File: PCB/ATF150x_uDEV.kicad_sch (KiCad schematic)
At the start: 14 parts, among them J1 Altera JTAG-A+VPP, J2 VERT, J3 VERT, U1 ATF150x-xAx44

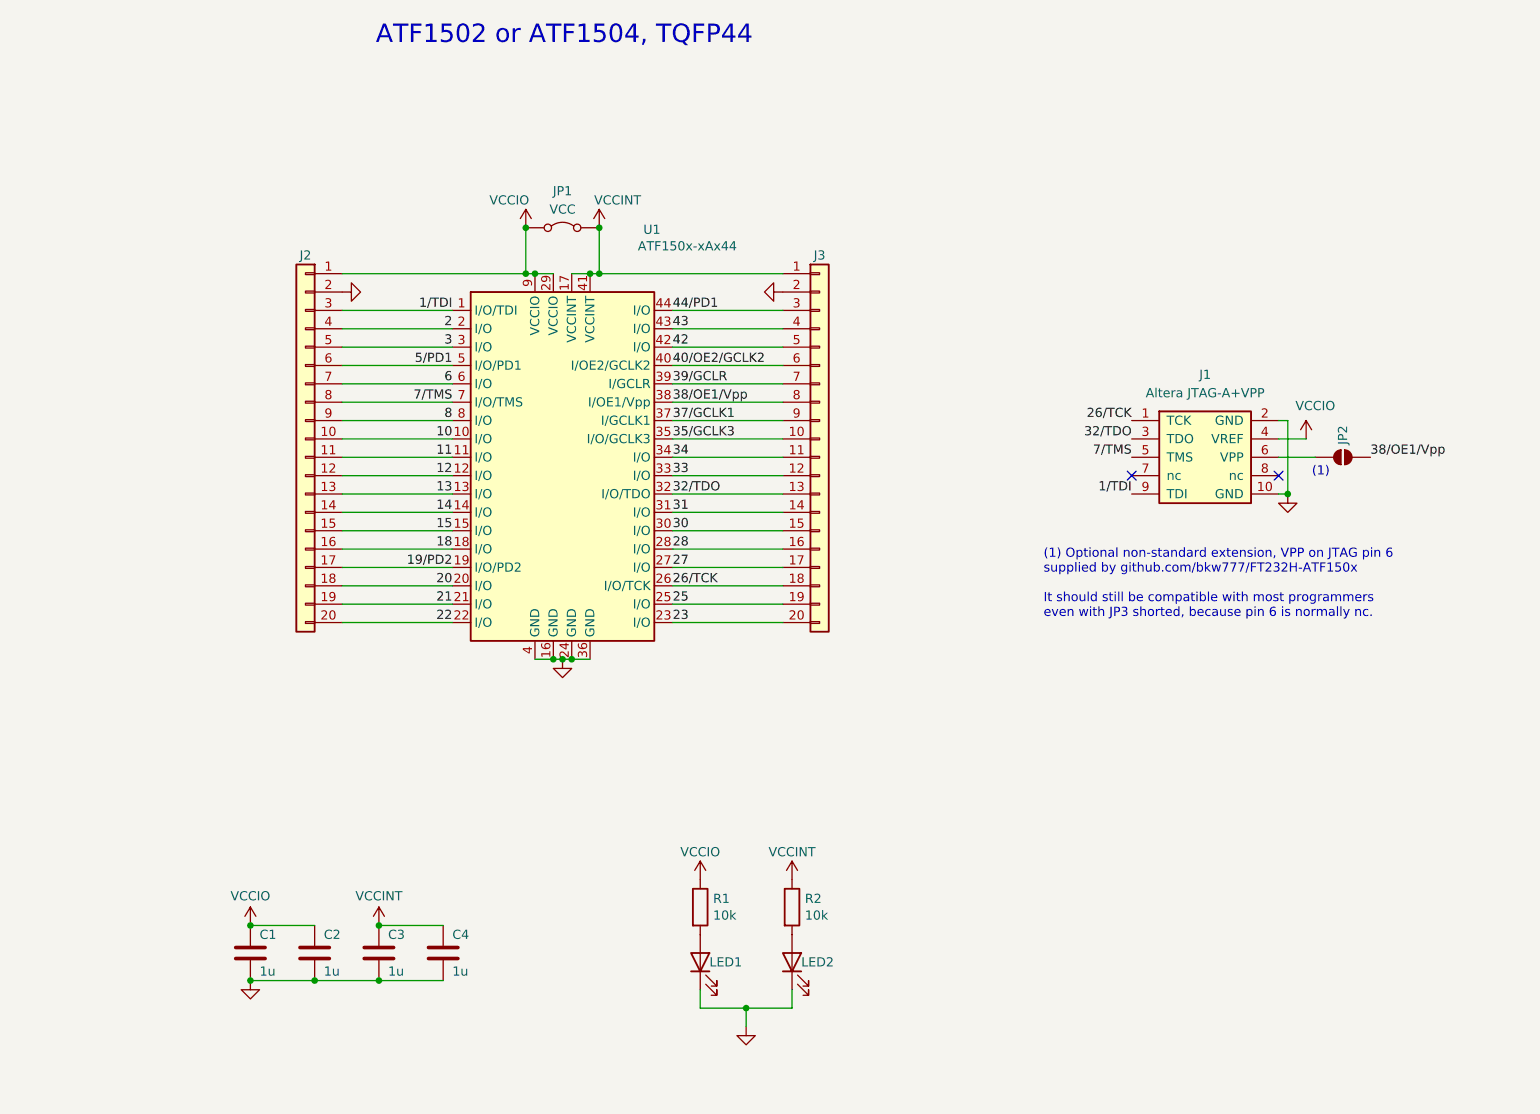
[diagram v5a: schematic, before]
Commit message: update link in comment in sch
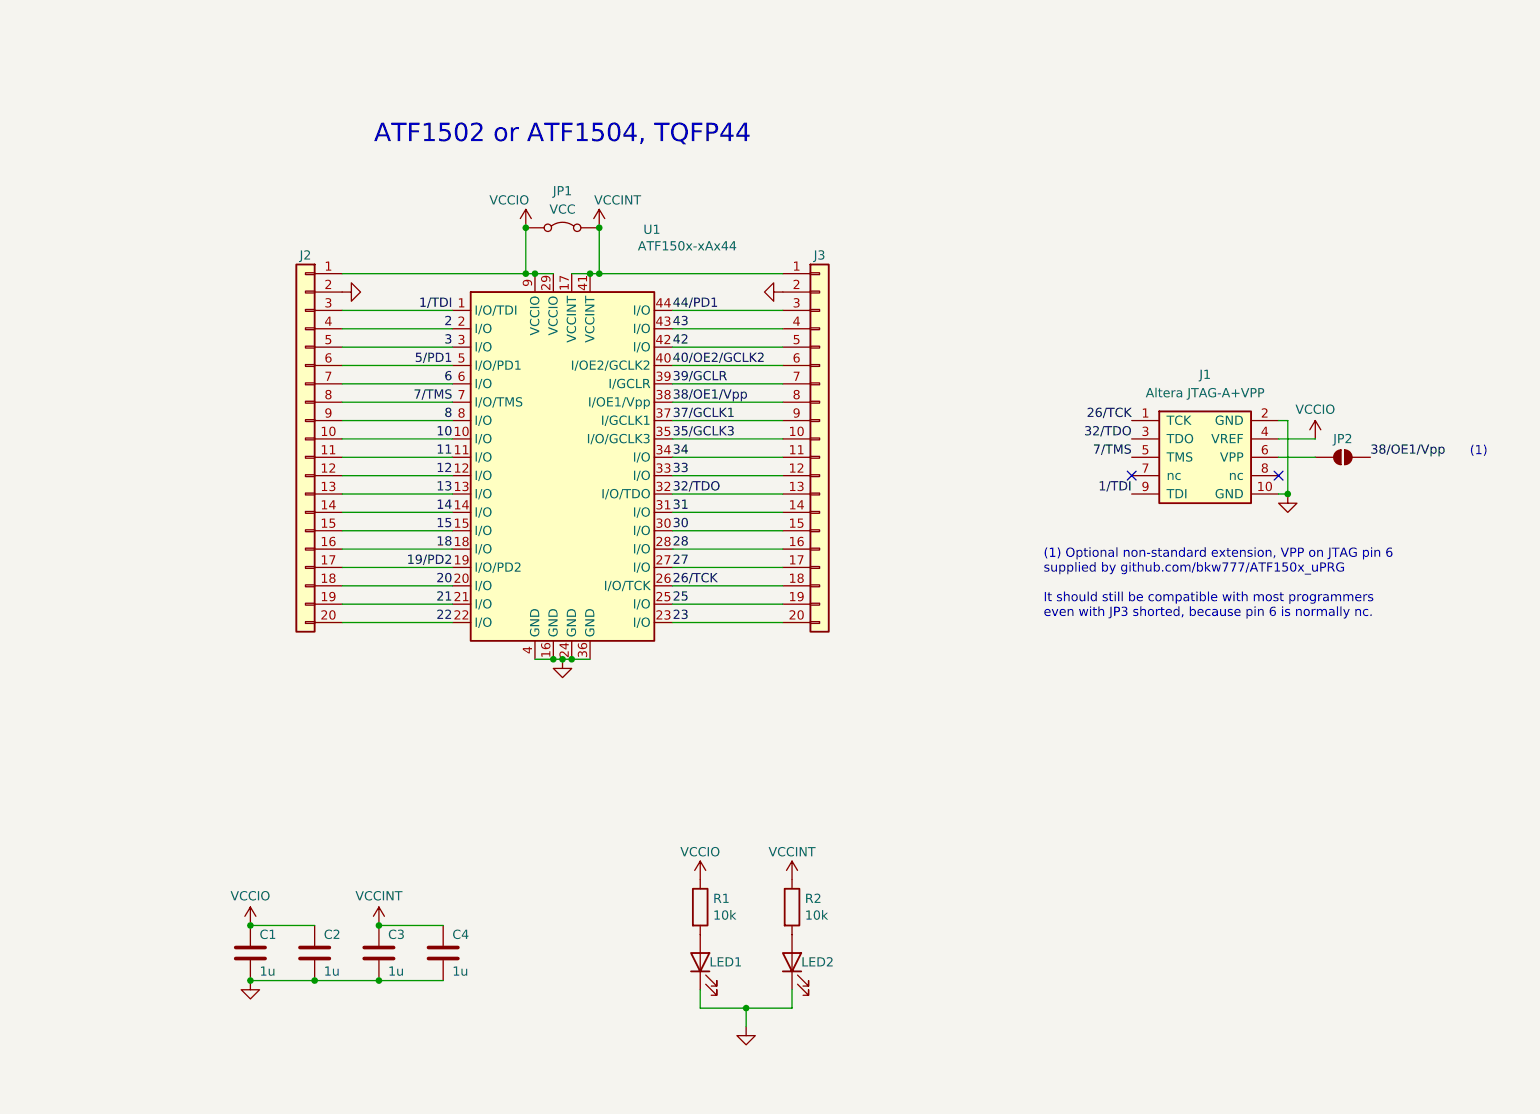
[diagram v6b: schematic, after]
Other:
- note added: "(1) Optional non-standard extension, VPP on JTAG pin 6 supplied by github.com/bkw777/ATF150x_uPRG It should still be compatible with most programmers even with JP3 shorted, because pin 6 is normally nc."
- note removed: "(1) Optional non-standard extension, VPP on JTAG pin 6 supplied by github.com/bkw777/FT232H-ATF150x It should still be compatible with most programmers even with JP3 shorted, because pin 6 is normally nc."
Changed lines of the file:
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@@
 	(wire
 		(pts
-			(xy 217.17 86.36) (xy 213.36 86.36)
+			(xy 218.44 86.36) (xy 213.36 86.36)
 		)
 		(stroke
@@
 	(text "(1)"
 		(exclude_from_sim no)
-		(at 219.202 90.932 0)
+		(at 241.046 88.138 0)
 		(effects
 			(font
@@
 	(text "ATF1502 or ATF1504, TQFP44\n"
 		(exclude_from_sim no)
-		(at 114.554 32.004 0)
+		(at 114.3 45.72 0)
 		(effects
 			(font
@@
 		)
 	)
-	(text "(1) Optional non-standard extension, VPP on JTAG pin 6\nsupplied by github.com/bkw777/FT232H-ATF150x\n\nIt should still be compatible with most programmers\neven with JP3 shorted, because pin 6 is normally nc."
+	(text "(1) Optional non-standard extension, VPP on JTAG pin 6\nsupplied by github.com/bkw777/ATF150x_uPRG\n\nIt should still be compatible with most programmers\neven with JP3 shorted, because pin 6 is normally nc."
 		(exclude_from_sim no)
 		(at 180.848 111.252 0)
@@
 		(dnp no)
 		(property "Reference" "JP2"
-			(at 222.25 87.1728 90)
-			(effects
-				(font
-					(size 1.27 1.27)
-				)
-				(justify left)
+			(at 222.25 86.36 0)
+			(effects
+				(font
+					(size 1.27 1.27)
+				)
 			)
 		)
@@
 	(symbol
 		(lib_id "power:VCC")
-		(at 217.17 86.36 0)
+		(at 218.44 86.36 0)
 		(unit 1)
 		(exclude_from_sim no)
@@
 		(dnp no)
 		(property "Reference" "#PWR010"
-			(at 217.17 90.17 0)
+			(at 218.44 90.17 0)
 			(effects
 				(font
@@
 		)
 		(property "Value" "VCCIO"
-			(at 218.44 81.788 0)
+			(at 218.44 82.296 0)
 			(effects
 				(font
@@
 		)
 		(property "Footprint" ""
-			(at 217.17 86.36 0)
+			(at 218.44 86.36 0)
 			(effects
 				(font
@@
 		)
 		(property "Datasheet" ""
-			(at 217.17 86.36 0)
+			(at 218.44 86.36 0)
 			(effects
 				(font
@@
 		)
 		(property "Description" "Power symbol creates a global label with name \"VCC\""
-			(at 217.17 86.36 0)
-			(effects
-				(font
+			(at 218.44 86.36 0)
+			(effects
+				(font

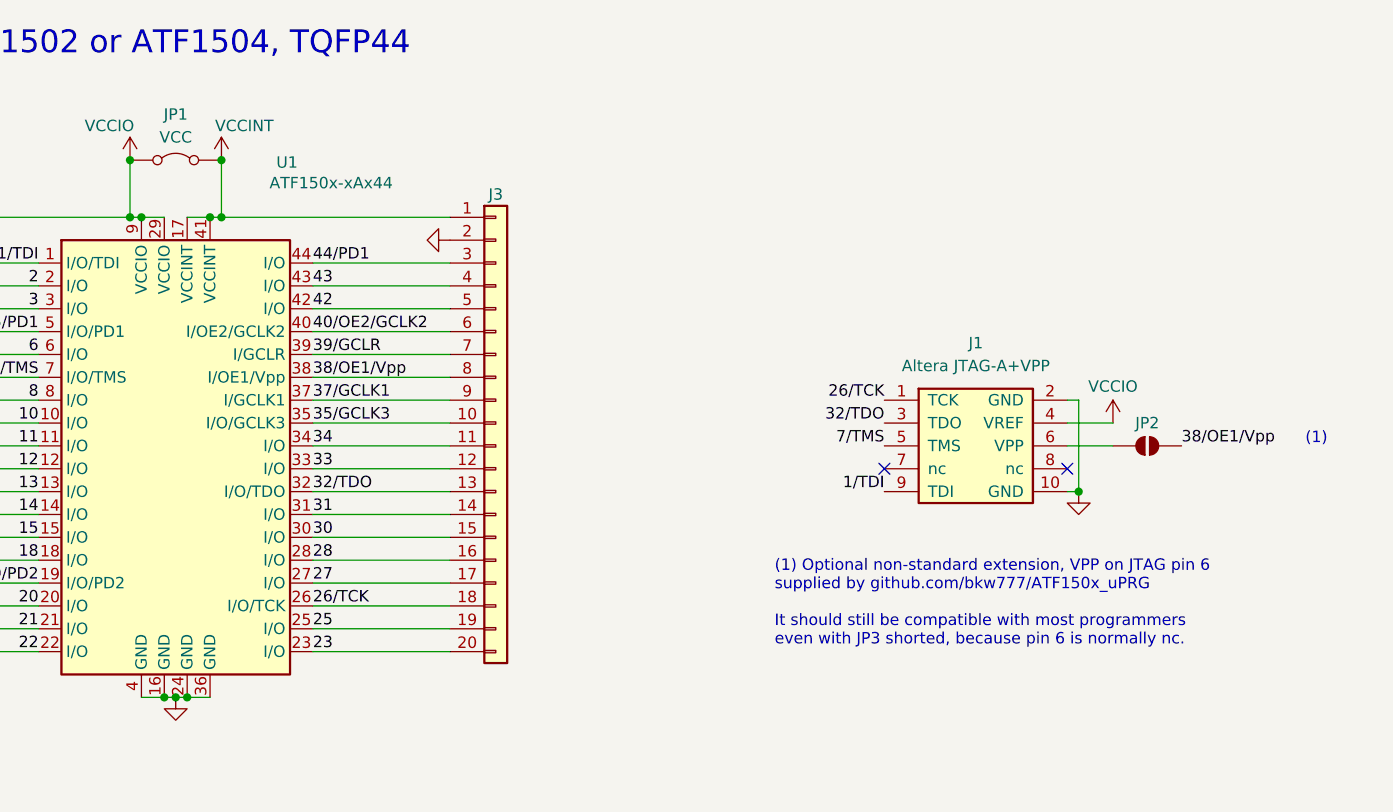
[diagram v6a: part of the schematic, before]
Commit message: correct pin 44 label, silkscreen, pics, move vpp jumper
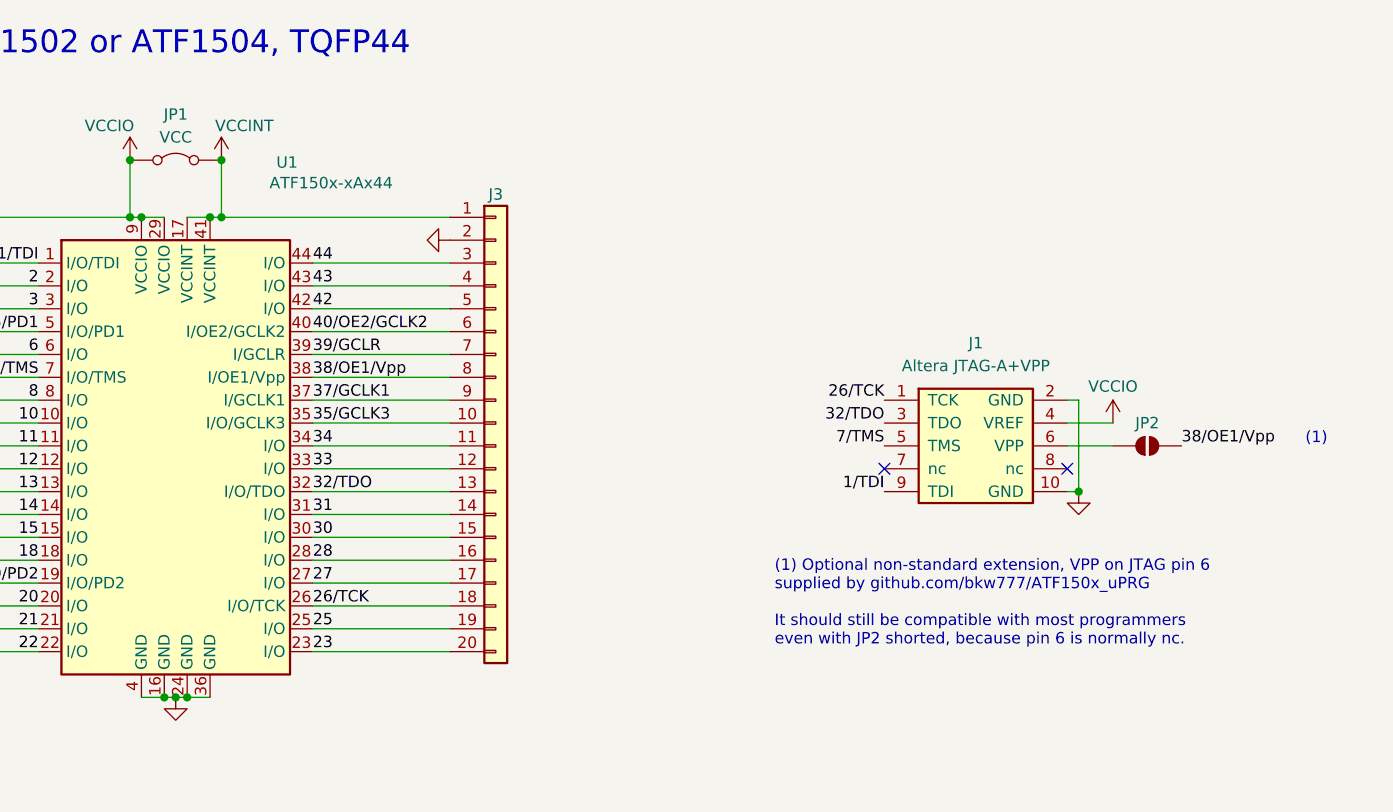
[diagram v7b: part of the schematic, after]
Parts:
- J2, J3: value VERT -> 1x20x2.54mm
- JP2: value DNP -> VPP; symbol Jumper:SolderJumper_2_Open -> 000_LOCAL:SolderJumper_2_Open; now left out of the parts list
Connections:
- net 44/PD1 renamed 44
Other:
- note added: "(1) Optional non-standard extension, VPP on JTAG pin 6 supplied by github.com/bkw777/ATF150x_uPRG It should still be compatible with most programmers even with JP2 shorted, because pin 6 is normally nc."
- note removed: "(1) Optional non-standard extension, VPP on JTAG pin 6 supplied by github.com/bkw777/ATF150x_uPRG It should still be compatible with most programmers even with JP3 shorted, because pin 6 is normally nc."
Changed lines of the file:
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@@
 (kicad_sch
-	(version 20231120)
+	(version 20250114)
 	(generator "eeschema")
-	(generator_version "8.0")
+	(generator_version "9.0")
 	(paper "A4")
 	(title_block
 		(title "ATF150x_uDEV")
-		(date "2024-07-26")
+		(date "2026-02-27")
 		(rev "006")
 		(company "Brian K. White")
@@
 		(comment 2 "github.com/bkw777/ATF150x_uDEV")
 	)
+	(text "(1)"
+		(exclude_from_sim no)
+		(at 241.046 88.138 0)
+		(effects
+			(font
+				(size 1.27 1.27)
+			)
+		)
+	)
+	(text "ATF1502 or ATF1504, TQFP44\n"
+		(exclude_from_sim no)
+		(at 114.3 45.72 0)
+		(effects
+			(font
+				(size 2.54 2.54)
+			)
+			(justify bottom)
+		)
+	)
+	(text "(1) Optional non-standard extension, VPP on JTAG pin 6\nsupplied by github.com/bkw777/ATF150x_uPRG\n\nIt should still be compatible with most programmers\neven with JP2 shorted, because pin 6 is normally nc."
+		(exclude_from_sim no)
+		(at 180.848 111.252 0)
+		(effects
+			(font
+				(size 1.27 1.27)
+			)
+			(justify left bottom)
+		)
+	)
 	(junction
 		(at 118.11 63.5)
@@
 		)
 	)
-	(text "(1)"
-		(exclude_from_sim no)
-		(at 241.046 88.138 0)
-		(effects
-			(font
-				(size 1.27 1.27)
-			)
-		)
-	)
-	(text "ATF1502 or ATF1504, TQFP44\n"
-		(exclude_from_sim no)
-		(at 114.3 45.72 0)
-		(effects
-			(font
-				(size 2.54 2.54)
-			)
-			(justify bottom)
-		)
-	)
-	(text "(1) Optional non-standard extension, VPP on JTAG pin 6\nsupplied by github.com/bkw777/ATF150x_uPRG\n\nIt should still be compatible with most programmers\neven with JP3 shorted, because pin 6 is normally nc."
-		(exclude_from_sim no)
-		(at 180.848 111.252 0)
-		(effects
-			(font
-				(size 1.27 1.27)
-			)
-			(justify left bottom)
-		)
-	)
 	(label "13"
 		(at 99.06 93.98 180)
-		(fields_autoplaced yes)
 		(effects
 			(font
@@
 	(label "26{slash}TCK"
 		(at 129.54 106.68 0)
-		(fields_autoplaced yes)
 		(effects
 			(font
@@
 	(label "14"
 		(at 99.06 96.52 180)
-		(fields_autoplaced yes)
 		(effects
 			(font
@@
 	(label "6"
 		(at 99.06 78.74 180)
-		(fields_autoplaced yes)
 		(effects
 			(font
@@
 	(label "38{slash}OE1{slash}Vpp"
 		(at 226.06 88.9 0)
-		(fields_autoplaced yes)
 		(effects
 			(font
@@
 	(label "23"
 		(at 129.54 111.76 0)
-		(fields_autoplaced yes)
 		(effects
 			(font
@@
 	(label "35{slash}GCLK3"
 		(at 129.54 86.36 0)
-		(fields_autoplaced yes)
 		(effects
 			(font
@@
 	(label "33"
 		(at 129.54 91.44 0)
-		(fields_autoplaced yes)
 		(effects
 			(font
@@
 	(label "5{slash}PD1"
 		(at 99.06 76.2 180)
-		(fields_autoplaced yes)
 		(effects
 			(font
@@
 	(label "42"
 		(at 129.54 73.66 0)
-		(fields_autoplaced yes)
 		(effects
 			(font
@@
 	(label "7{slash}TMS"
 		(at 99.06 81.28 180)
-		(fields_autoplaced yes)
 		(effects
 			(font
@@
 	(label "28"
 		(at 129.54 101.6 0)
-		(fields_autoplaced yes)
 		(effects
 			(font
@@
 	(label "10"
 		(at 99.06 86.36 180)
-		(fields_autoplaced yes)
 		(effects
 			(font
@@
 	(label "38{slash}OE1{slash}Vpp"
 		(at 129.54 81.28 0)
-		(fields_autoplaced yes)
 		(effects
 			(font
@@
 		)
 	)
-	(label "44{slash}PD1"
+	(label "44"
 		(at 129.54 68.58 0)
-		(fields_autoplaced yes)
 		(effects
 			(font
@@
 	(label "32{slash}TDO"
 		(at 193.04 86.36 180)
-		(fields_autoplaced yes)
 		(effects
 			(font
@@
 	(label "40{slash}OE2{slash}GCLK2"
 		(at 129.54 76.2 0)
-		(fields_autoplaced yes)
 		(effects
 			(font
@@
 	(label "37{slash}GCLK1"
 		(at 129.54 83.82 0)
-		(fields_autoplaced yes)
 		(effects
 			(font
@@
 	(label "30"
 		(at 129.54 99.06 0)
-		(fields_autoplaced yes)
 		(effects
 			(font
@@
 	(label "34"
 		(at 129.54 88.9 0)
-		(fields_autoplaced yes)
 		(effects
 			(font
@@
 	(label "20"
 		(at 99.06 106.68 180)
-		(fields_autoplaced yes)
 		(effects
 			(font
@@
 	(label "22"
 		(at 99.06 111.76 180)
-		(fields_autoplaced yes)
 		(effects
 			(font
@@
 	(label "26{slash}TCK"
 		(at 193.04 83.82 180)
-		(fields_autoplaced yes)
 		(effects
 			(font
@@
 	(label "27"
 		(at 129.54 104.14 0)
-		(fields_autoplaced yes)
 		(effects
 			(font
@@
 	(label "8"
 		(at 99.06 83.82 180)
-		(fields_autoplaced yes)
 		(effects
 			(font
@@
 	(label "18"
 		(at 99.06 101.6 180)
-		(fields_autoplaced yes)
 		(effects
 			(font
@@
 	(label "19{slash}PD2"
 		(at 99.06 104.14 180)
-		(fields_autoplaced yes)
 		(effects
 			(font
@@
 	(label "11"
 		(at 99.06 88.9 180)
-		(fields_autoplaced yes)
 		(effects
 			(font
@@
 	(label "1{slash}TDI"
 		(at 193.04 93.98 180)
-		(fields_autoplaced yes)
 		(effects
 			(font
@@
 	(label "39{slash}GCLR"
 		(at 129.54 78.74 0)
-		(fields_autoplaced yes)
 		(effects
 			(font
@@
 	(label "25"
 		(at 129.54 109.22 0)
-		(fields_autoplaced yes)
 		(effects
 			(font
@@
 	(label "31"
 		(at 129.54 96.52 0)
-		(fields_autoplaced yes)
 		(effects
 			(font
@@
 	(label "3"
 		(at 99.06 73.66 180)
-		(fields_autoplaced yes)
 		(effects
 			(font
@@
 	(label "43"
 		(at 129.54 71.12 0)
-		(fields_autoplaced yes)
 		(effects
 			(font
@@
 	(label "1{slash}TDI"
 		(at 99.06 68.58 180)
-		(fields_autoplaced yes)
 		(effects
 			(font
@@
 	(label "15"
 		(at 99.06 99.06 180)
-		(fields_autoplaced yes)
 		(effects
 			(font
@@
 	(label "12"
 		(at 99.06 91.44 180)
-		(fields_autoplaced yes)
 		(effects
 			(font
@@
 	(label "32{slash}TDO"
 		(at 129.54 93.98 0)
-		(fields_autoplaced yes)
 		(effects
 			(font
@@
 	(label "21"
 		(at 99.06 109.22 180)
-		(fields_autoplaced yes)
 		(effects
 			(font
@@
 	(label "2"
 		(at 99.06 71.12 180)
-		(fields_autoplaced yes)
 		(effects
 			(font
@@
 	(label "7{slash}TMS"
 		(at 193.04 88.9 180)
-		(fields_autoplaced yes)
 		(effects
 			(font
@@
 			)
 		)
-		(property "Value" "VERT"
+		(property "Value" "1x20x2.54mm"
 			(at 80.8228 115.1636 0)
 			(effects
@@
 			)
 		)
-		(property "Value" "VERT"
+		(property "Value" "1x20x2.54mm"
 			(at 147.7772 60.2996 0)
 			(effects
@@
 	)
 	(symbol
-		(lib_id "Jumper:SolderJumper_2_Open")
+		(lib_id "000_LOCAL:SolderJumper_2_Open")
 		(at 222.25 88.9 0)
 		(unit 1)
 		(exclude_from_sim no)
-		(in_bom yes)
+		(in_bom no)
 		(on_board yes)
 		(dnp no)
@@
 			)
 		)
-		(property "Value" "DNP"
+		(property "Value" "VPP"
 			(at 223.393 87.1728 90)
 			(effects
@@
 			)
 		)
-		(property "Description" ""
+		(property "Description" "Solder Jumper, 2-pole, open"
 			(at 222.25 88.9 0)
 			(effects
@@
 		)
 	)
+	(embedded_fonts no)
 )
